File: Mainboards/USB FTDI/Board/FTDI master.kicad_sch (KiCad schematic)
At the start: 52 parts, among them IC1 NCP1117ST, IC10 FT232RL, IC2 MCP1700T-1802E, IC3 CRE1S0505SC, IC4 IL0512S, IC5 IRF7416, IC7 MAX14932, IC8 MAX14932, IC9 MAX14932, J1 USB_C_Receptacle_USB2.0, X2 AKL18X-04W, X3 IDC-Header_2x05_P2.54mm_Verti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, X4 ALLSERIALMASTERM

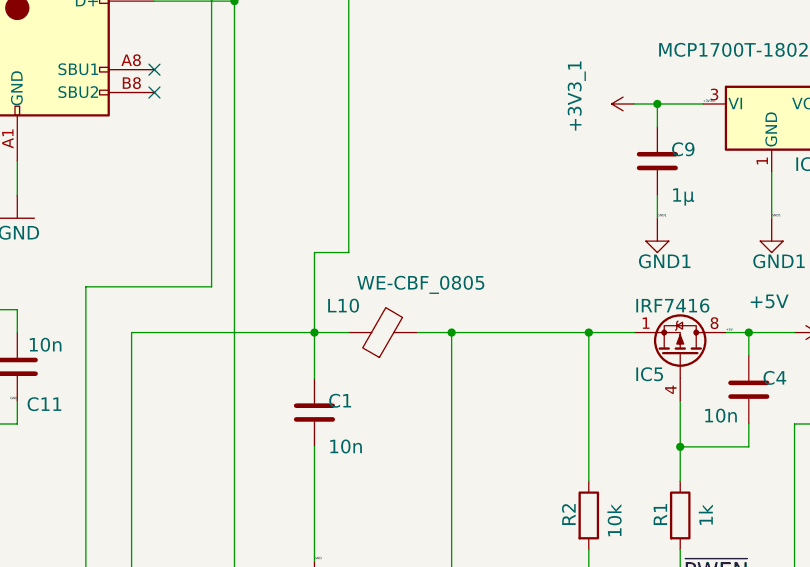
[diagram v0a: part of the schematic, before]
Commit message: Migrate to new KiCad Version
Add SMA connector front
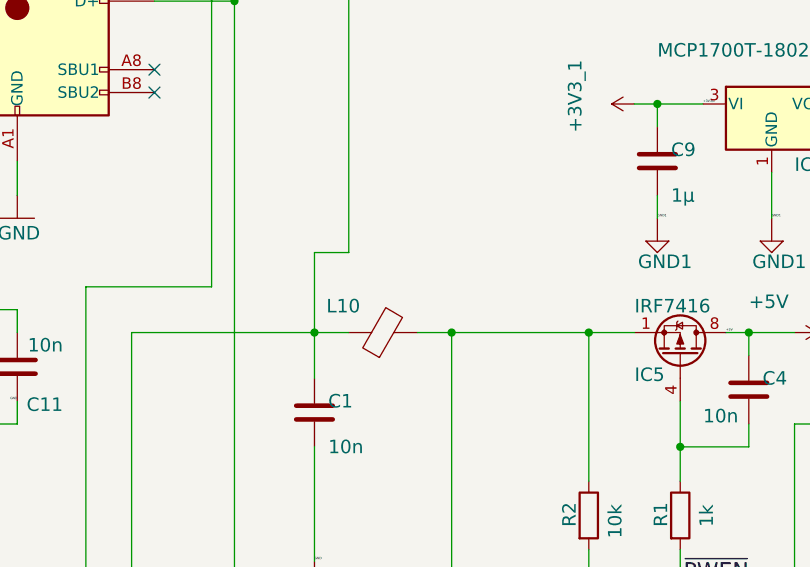
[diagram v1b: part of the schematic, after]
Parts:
- C1, C11, C4: LSCS order # (none) -> C1710
- C10, C9: LSCS order # (none) -> C111768
- C13, C3: LSCS order # (none) -> C90544
- C15, C16, C17, C18, C19, C2, C5, C7, C8: footprint Capacitor_SMD:C_0805_2012Metric -> Capacitor_SMD:C_0603_1608Metric; LSCS order # (none) -> C14663
- C6: LSCS order # (none) -> C2918489
- D1: LSCS order # (none) -> C5197386
- IC1: LSCS order # (none) -> C26537
- IC10: LSCS order # (none) -> C8690
- IC2: LSCS order # (none) -> C150796
- IC5: LSCS order # (none) -> C5261058
- IC7, IC8, IC9: value MAX14932 -> ADuM142E0BRQZ-RL7; footprint Package_SO:SOIC-16_3.9x9.9mm_P1.27mm -> Package_SO:QSOP-16_3.9x4.9mm_P0.635mm; symbol AllSerial:MAX14932 -> AllSerial:ADuM142; LSCS order # (none) -> C208656
- L10: value WE-CBF_0805 -> ~; LSCS order # (none) -> C76817
- LED1: LSCS order # (none) -> C2986058
- LED2: LSCS order # (none) -> C2986030
- LED3: LSCS order # (none) -> C2986060
- LED4: LSCS order # (none) -> C2986063
- R1: LSCS order # (none) -> C17513
- R10, R11, R12, R2, R6, R7: LSCS order # (none) -> C17414
- R13, R14: LSCS order # (none) -> C27834
- R3, R4, R8, R9: LSCS order # (none) -> C93657
- R5: LSCS order # (none) -> C3152182
- X3: LSCS order # (none) -> C429962
- X4: LSCS order # (none) -> C124406

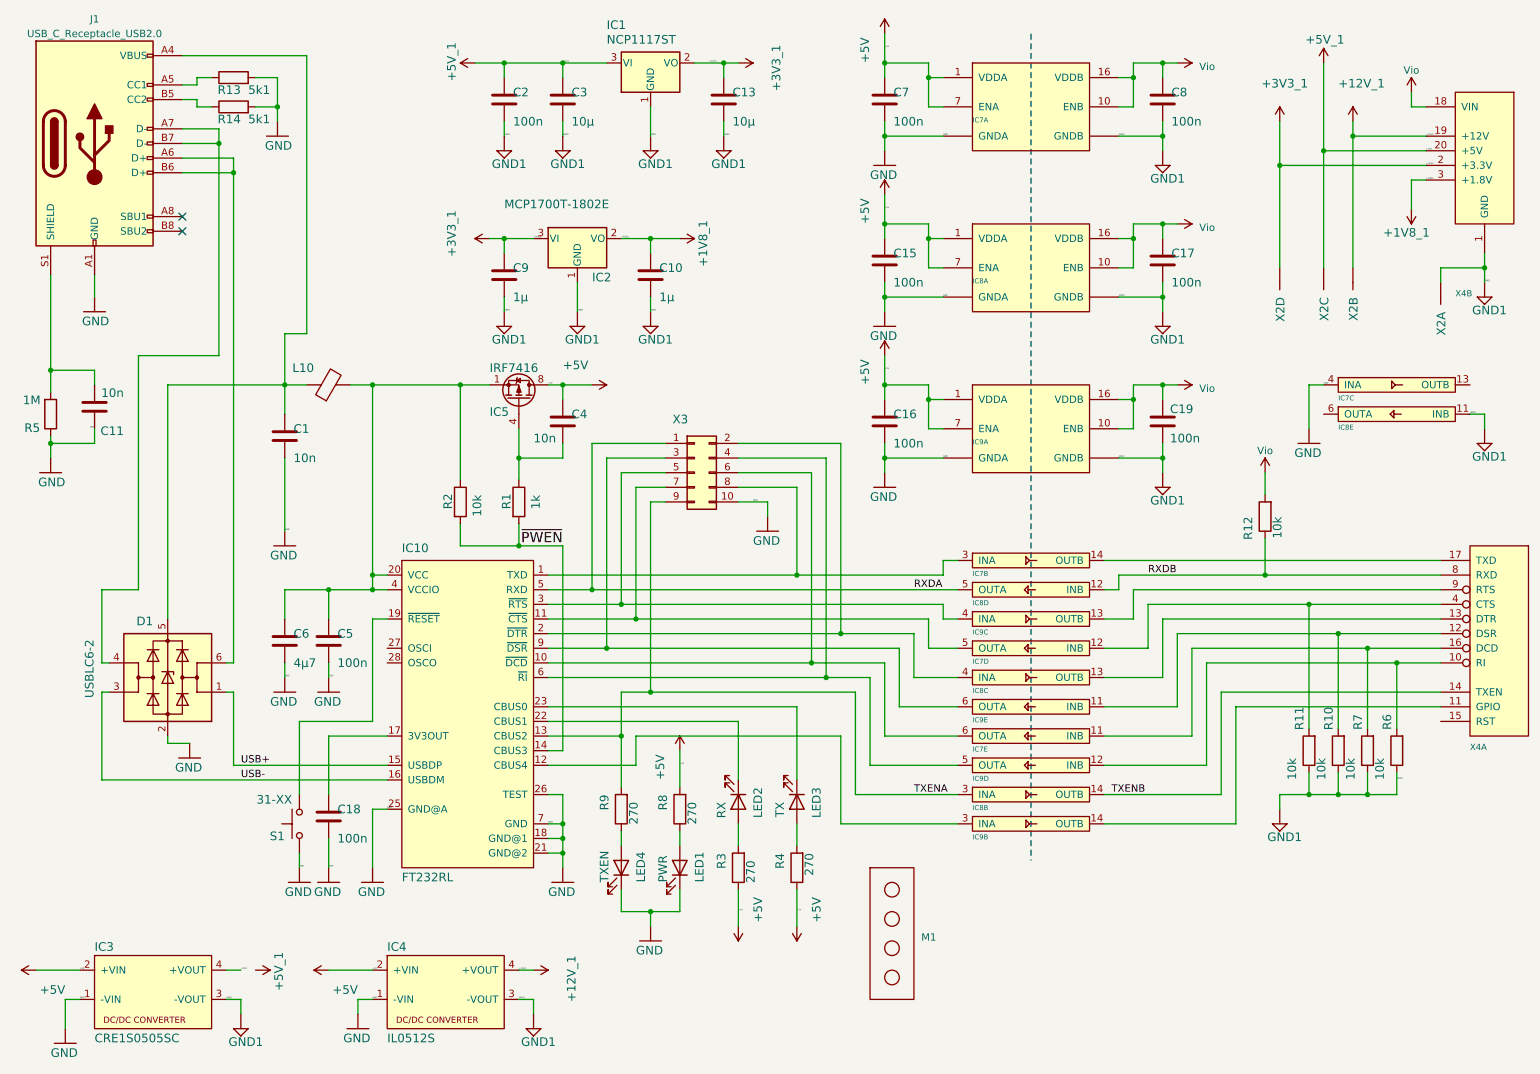
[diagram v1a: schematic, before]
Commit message: Update TTY CL slave board
Add ESP32 S3 WiFi MasterBoard
Update libs
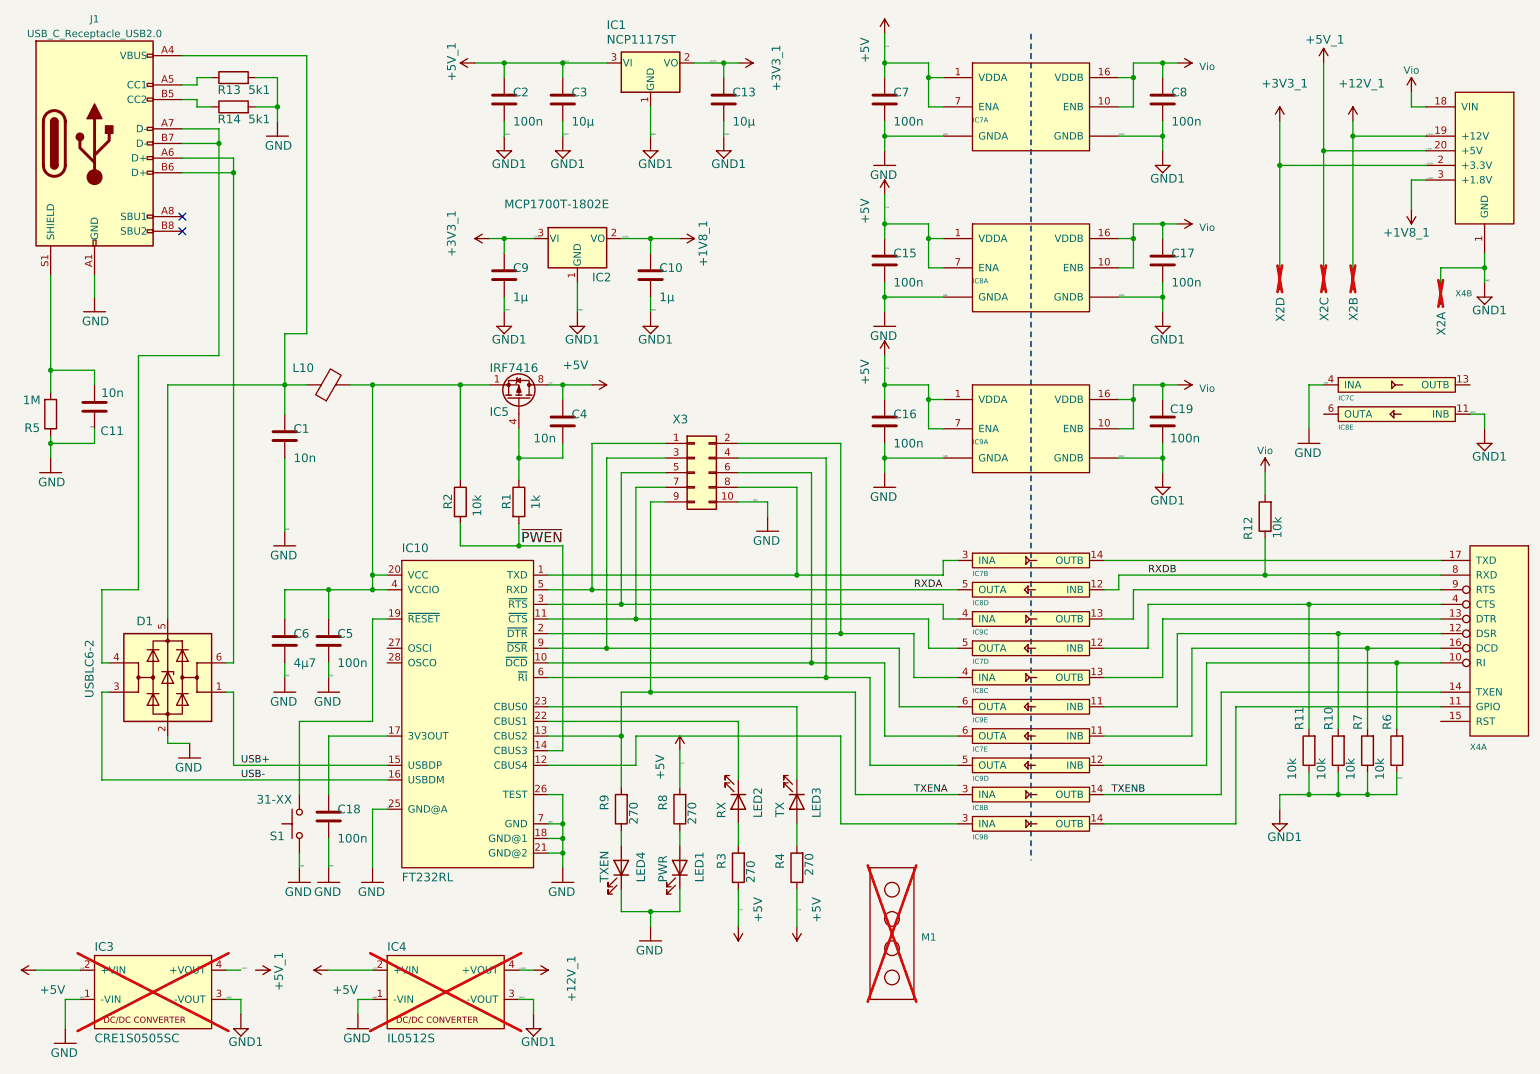
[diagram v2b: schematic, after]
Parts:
- C1, C11, C4: LCSC (none) -> C1710; LSCS order # C1710 -> (none)
- C10, C9: LCSC (none) -> C111768; LSCS order # C111768 -> (none)
- C13, C3: LCSC (none) -> C90544; LSCS order # C90544 -> (none)
- C15, C16, C17, C18, C19, C2, C5, C7, C8: LCSC (none) -> C14663; LSCS order # C14663 -> (none)
- C6: LCSC (none) -> C2918489; LSCS order # C2918489 -> (none)
- D1: LCSC (none) -> C5197386; LSCS order # C5197386 -> (none)
- IC1: LCSC (none) -> C26537; LSCS order # C26537 -> (none)
- IC10: LCSC (none) -> C8690; LSCS order # C8690 -> (none)
- IC2: LCSC (none) -> C150796; LSCS order # C150796 -> (none)
- IC3, IC4, M1, X2: now not fitted
- IC5: LCSC (none) -> C5261058; LSCS order # C5261058 -> (none)
- IC7, IC8, IC9: LCSC (none) -> C208656; LSCS order # C208656 -> (none)
- J1: LCSC (none) -> C2927037
- L10: LCSC (none) -> C76817; LSCS order # C76817 -> (none)
- LED1: LCSC (none) -> C2986058; LSCS order # C2986058 -> (none)
- LED2: LCSC (none) -> C2986030; LSCS order # C2986030 -> (none)
- LED3: LCSC (none) -> C2986060; LSCS order # C2986060 -> (none)
- LED4: LCSC (none) -> C2986063; LSCS order # C2986063 -> (none)
- R1: LCSC (none) -> C17513; LSCS order # C17513 -> (none)
- R10, R11, R12, R2, R6, R7: LCSC (none) -> C17414; LSCS order # C17414 -> (none)
- R13, R14: LCSC (none) -> C27834; LSCS order # C27834 -> (none)
- R3, R4, R8, R9: LCSC (none) -> C93657; LSCS order # C93657 -> (none)
- R5: LCSC (none) -> C3152182; LSCS order # C3152182 -> (none)
- X3: LCSC (none) -> C429962; LSCS order # C429962 -> (none)
- X4: LCSC (none) -> C124406; LSCS order # C124406 -> (none)
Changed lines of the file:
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@@
 			)
 		)
-		(property "LSCS order #" "C93657"
+		(property "LCSC" "C93657"
 			(at 129.54 154.94 0)
 			(effects
@@
 			)
 		)
-		(property "LSCS order #" "C17414"
+		(property "LCSC" "C17414"
 			(at 254 144.78 0)
 			(effects
@@
 			)
 		)
-		(property "LSCS order #" "C93657"
+		(property "LCSC" "C93657"
 			(at 119.38 154.94 0)
 			(effects
@@
 			)
 		)
-		(property "LSCS order #" "C14663"
+		(property "LCSC" "C14663"
 			(at 213.36 59.69 0)
 			(effects
@@
 			)
 		)
-		(property "LSCS order #" "C26537"
+		(property "LCSC" "C26537"
 			(at 124.46 25.4 0)
 			(effects
@@
 			)
 		)
-		(property "LSCS order #" "C1710"
+		(property "LCSC" "C1710"
 			(at 27.94 85.09 0)
 			(effects
@@
 			)
 		)
-		(property "LSCS order #" "C2986030"
+		(property "LCSC" "C2986030"
 			(at 139.7 153.67 0)
 			(effects
@@
 			)
 		)
-		(property "LSCS order #" "C208656"
+		(property "LCSC" "C208656"
 			(at 190.5 127 0)
 			(effects
@@
 			)
 		)
-		(property "LSCS order #" "C208656"
+		(property "LCSC" "C208656"
 			(at 190.5 142.24 0)
 			(effects
@@
 			)
 		)
-		(property "LSCS order #" "C208656"
+		(property "LCSC" "C208656"
 			(at 190.5 111.76 0)
 			(effects
@@
 			)
 		)
-		(property "LSCS order #" "C208656"
+		(property "LCSC" "C208656"
 			(at 254 81.28 0)
 			(effects
@@
 			)
 		)
-		(property "LSCS order #" "C208656"
+		(property "LCSC" "C208656"
 			(at 190.5 33.02 0)
 			(effects
@@
 			)
 		)
-		(property "LSCS order #" "C17414"
+		(property "LCSC" "C17414"
 			(at 238.76 144.78 0)
 			(effects
@@
 			)
 		)
-		(property "LSCS order #" "C124406"
+		(property "LCSC" "C124406"
 			(at 271.78 127 0)
 			(effects
@@
 			)
 		)
-		(property "LSCS order #" "C124406"
+		(property "LCSC" "C124406"
 			(at 269.24 48.26 0)
 			(effects
@@
 			)
 		)
-		(property "LSCS order #" "C14663"
+		(property "LCSC" "C14663"
 			(at 165.1 87.63 0)
 			(effects
@@
 			)
 		)
-		(property "LSCS order #" "C2918489"
+		(property "LCSC" "C2918489"
 			(at 60.96 125.73 0)
 			(effects
@@
 			)
 		)
-		(property "LSCS order #" "C90544"
+		(property "LCSC" "C90544"
 			(at 109.22 31.75 0)
 			(effects
@@
 			)
 		)
-		(property "LSCS order #" "C2986060"
+		(property "LCSC" "C2986060"
 			(at 149.86 153.67 0)
 			(effects
@@
 			)
 		)
-		(property "LSCS order #" "C5261058"
+		(property "LCSC" "C5261058"
 			(at 101.6 83.82 0)
 			(effects
@@
 			)
 		)
-		(property "LSCS order #" "C14663"
+		(property "LCSC" "C14663"
 			(at 68.58 125.73 0)
 			(effects
@@
 			)
 		)
-		(property "LSCS order #" "C14663"
+		(property "LCSC" "C14663"
 			(at 213.36 87.63 0)
 			(effects
@@
 			)
 		)
-		(property "LSCS order #" "C5197386"
+		(property "LCSC" "C5197386"
 			(at 40.64 132.08 0)
 			(effects
@@
 			)
 		)
-		(property "LSCS order #" "C150796"
+		(property "LCSC" "C150796"
 			(at 111.76 55.88 0)
 			(effects
@@
 			)
 		)
-		(property "LSCS order #" "C1710"
+		(property "LCSC" "C1710"
 			(at 109.22 87.63 0)
 			(effects
@@
 			)
 		)
-		(property "LSCS order #" "C111768"
+		(property "LCSC" "C111768"
 			(at 99.06 62.23 0)
 			(effects
@@
 			)
 		)
-		(property "LSCS order #" "C93657"
+		(property "LCSC" "C93657"
 			(at 149.86 165.1 0)
 			(effects
@@
 			)
 		)
-		(property "LSCS order #" "C17414"
+		(property "LCSC" "C17414"
 			(at 91.44 101.6 0)
 			(effects
@@
 			)
 		)
-		(property "LSCS order #" "C8690"
+		(property "LCSC" "C8690"
 			(at 91.44 137.16 0)
 			(effects
@@
 			)
 		)
-		(property "LSCS order #" "C93657"
+		(property "LCSC" "C93657"
 			(at 139.7 165.1 0)
 			(effects
@@
 			)
 		)
-		(property "LSCS order #" "C14663"
+		(property "LCSC" "C14663"
 			(at 165.1 59.69 0)
 			(effects
@@
 			)
 		)
-		(property "LSCS order #" "C14663"
+		(property "LCSC" "C14663"
 			(at 165.1 31.75 0)
 			(effects
@@
 			)
 		)
-		(property "LSCS order #" "C14663"
+		(property "LCSC" "C14663"
 			(at 99.06 31.75 0)
 			(effects
@@
 		(in_bom yes)
 		(on_board yes)
-		(dnp no)
+		(dnp yes)
 		(property "Reference" "IC3"
 			(at 27.94 179.705 0)
@@
 			)
 		)
-		(property "LSCS order #" "C2986058"
+		(property "LCSC" "C2986058"
 			(at 129.54 165.1 0)
 			(effects
@@
 			)
 		)
-		(property "LSCS order #" "C2986063"
+		(property "LCSC" "C2986063"
 			(at 119.38 165.1 0)
 			(effects
@@
 			)
 		)
-		(property "LSCS order #" "C17414"
+		(property "LCSC" "C17414"
 			(at 243.84 144.78 0)
 			(effects
@@
 			)
 		)
-		(property "LSCS order #" "C14663"
+		(property "LCSC" "C14663"
 			(at 213.36 31.75 0)
 			(effects
@@
 			)
 		)
-		(property "LSCS order #" "C76817"
+		(property "LCSC" "C76817"
 			(at 68.58 81.28 0)
 			(effects
@@
 			)
 		)
-		(property "LSCS order #" "C3152182"
+		(property "LCSC" "C3152182"
 			(at 20.32 86.36 0)
 			(effects
@@
 			)
 		)
-		(property "LSCS order #" "C429962"
+		(property "LCSC" "C429962"
 			(at 132.08 96.52 0)
 			(effects
@@
 			)
 		)
-		(property "LSCS order #" "C1710"
+		(property "LCSC" "C1710"
 			(at 60.96 90.17 0)
 			(effects
@@
 			)
 		)
-		(property "LSCS order #" "C90544"
+		(property "LCSC" "C90544"
 			(at 137.16 31.75 0)
 			(effects
@@
 			)
 		)
-		(property "LSCS order #" "C17513"
+		(property "LCSC" "C17513"
 			(at 101.6 101.6 0)
 			(effects
@@
 			)
 		)
-		(property "LSCS order #" "C17414"
+		(property "LCSC" "C17414"
 			(at 248.92 144.78 0)
 			(effects
@@
 		(in_bom yes)
 		(on_board yes)
-		(dnp no)
+		(dnp yes)
 		(property "Reference" "X2"
 			(at 232.918 66.04 0)
@@
 		(in_bom yes)
 		(on_board yes)
-		(dnp no)
+		(dnp yes)
 		(property "Reference" "X2"
 			(at 240.538 66.04 0)
@@
 		(in_bom yes)
 		(on_board yes)
-		(dnp no)
+		(dnp yes)
 		(property "Reference" "X2"
 			(at 245.618 66.04 0)
@@
 		(in_bom yes)
 		(on_board yes)
-		(dnp no)
+		(dnp yes)
 		(property "Reference" "X2"
 			(at 260.858 68.58 0)
@@
 			)
 		)
-		(property "LSCS order #" "C111768"
+		(property "LCSC" "C111768"
 			(at 124.46 62.23 0)
 			(effects
@@
 			)
 		)
-		(property "LSCS order #" "C208656"
+		(property "LCSC" "C208656"
 			(at 190.5 157.48 0)
 			(effects
@@
 			)
 		)
-		(property "LSCS order #" "C208656"
+		(property "LCSC" "C208656"
 			(at 190.5 121.92 0)
 			(effects
@@
 			)
 		)
-		(property "LSCS order #" "C208656"
+		(property "LCSC" "C208656"
 			(at 190.5 88.9 0)
 			(effects
@@
 			)
 		)
-		(property "LSCS order #" "C208656"
+		(property "LCSC" "C208656"
 			(at 190.5 147.32 0)
 			(effects
@@
 			)
 		)
-		(property "LSCS order #" "C208656"
+		(property "LCSC" "C208656"
 			(at 190.5 137.16 0)
 			(effects
@@
 			)
 		)
-		(property "LSCS order #" "C208656"
+		(property "LCSC" "C208656"
 			(at 254 86.36 0)
 			(effects
@@
 			)
 		)
-		(property "LSCS order #" "C208656"
+		(property "LCSC" "C208656"
 			(at 190.5 116.84 0)
 			(effects
@@
 			)
 		)
-		(property "LSCS order #" "C208656"
+		(property "LCSC" "C208656"
 			(at 190.5 132.08 0)
 			(effects
@@
 			)
 		)
-		(property "LSCS order #" "C208656"
+		(property "LCSC" "C208656"
 			(at 190.5 152.4 0)
 			(effects
@@
 			)
 		)
-		(property "LSCS order #" "C208656"
+		(property "LCSC" "C208656"
 			(at 190.5 60.96 0)
 			(effects
@@
 			)
 		)
-		(property "LSCS order #" "C17414"
+		(property "LCSC" "C17414"
 			(at 231.14 104.14 0)
 			(effects
@@
 		(in_bom yes)
 		(on_board yes)
-		(dnp no)
+		(dnp yes)
 		(property "Reference" "IC4"
 			(at 78.74 179.705 0)
@@
 			)
 		)
-		(property "LSCS order #" "C14663"
+		(property "LCSC" "C14663"
 			(at 68.58 156.21 0)
 			(effects
@@
 		(in_bom yes)
 		(on_board yes)
-		(dnp no)
+		(dnp yes)
 		(fields_autoplaced yes)
 		(property "Reference" "M1"
@@
 			)
 		)
-		(property "LSCS order #" "C27834"
+		(property "LCSC" "C27834"
 			(at 52.07 33.02 0)
 			(effects
@@
 			)
 		)
-		(property "LSCS order #" "C27834"
+		(property "LCSC" "C27834"
 			(at 52.07 27.94 0)
 			(effects
@@
 			(at 27.94 39.37 0)
 			(effects
+				(font
+					(size 1.27 1.27)
+				)
+				(hide yes)
+			)
+		)
+		(property "LCSC" "C2927037"
+			(at 27.94 39.37 0)
+			(effects
